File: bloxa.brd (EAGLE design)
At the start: 24.9 x 33.6 mm, 87 parts, among them CON1 PINHEAD_1X02-2.54, CON7 CON-4P-JST_GH-RA, CON8 CON-4P-JST_GH-RA, IC1 TPD3S014DBVR-SOT23-6, IC3 TJA1051, IC6 MCP9700, Q13 BUK9K6R2-40E,115, Q14 BUK9K6R2-40E,115, Q15 BUK9K6R2-40E,115

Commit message: updates
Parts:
- moved CON7 3.00 mm to (-4.50, -12.5)
- moved CON8 3.00 mm to (4.50, -12.5)
- renumbered PAD42 to BAT-, PAD43 to BAT+
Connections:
- removed net CAN2_LED1: R9.1
- removed net LED_BLUE: R11.2
- removed net LED_GREEN: R12.2
- removed net LED_RED: R13.2
- removed net N$3: BAT+.P$1, D1.C, D2.C
- net CAN1_LED: now also R9.1
- net GPIO1: now also CON1.2
- net PGND: now also CON1.1
- net RGB_LED_B: now also R11.2
- net RGB_LED_G: now also R12.2
- net RGB_LED_R: now also R13.2
- net VDC: now also BAT+.P$1, D1.C, D2.C

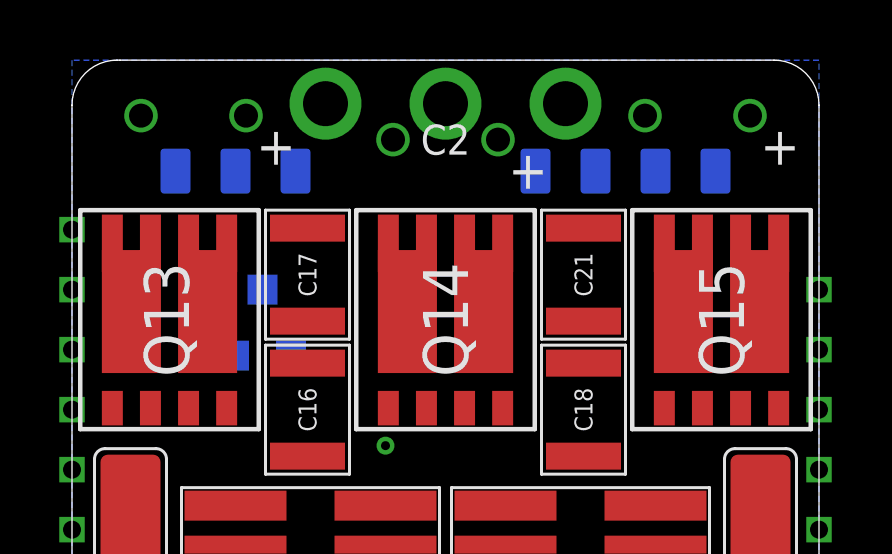
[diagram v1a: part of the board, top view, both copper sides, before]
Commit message: proper DRC and some polygons
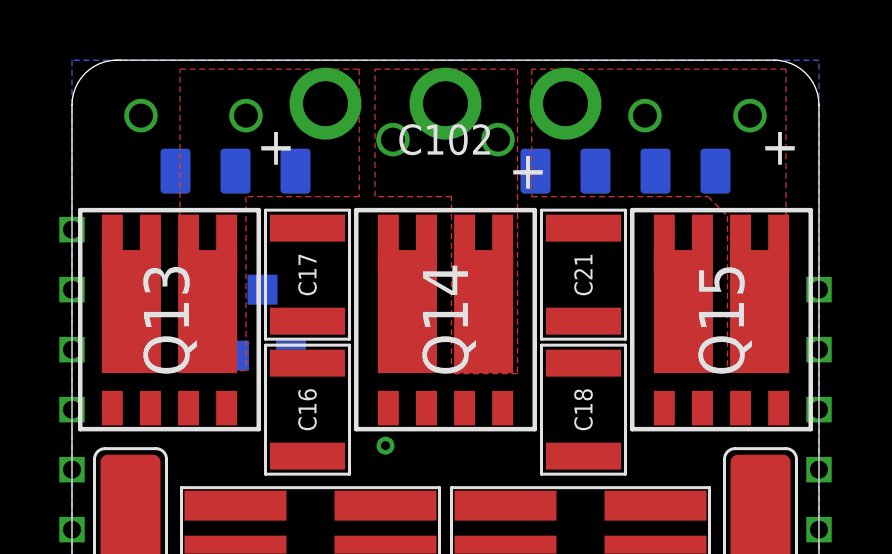
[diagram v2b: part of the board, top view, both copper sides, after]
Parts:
- renumbered C1 to C101, C2 to C102, C6 to C100
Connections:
- removed net VBAT: PAD3.P$1
- net VDC: now also PAD3.P$1
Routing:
- net VDDA: track 25.6 -> 0.00 mm
- net N$2: track 1.53 -> 0.00 mm
- net AGND: track 1.53 -> 0.00 mm
- added copper zone on layer 15, net PGND
- added copper zone on layer 1, net PHASE_A
- added copper zone on layer 1, net PHASE_B
- added copper zone on layer 1, net PHASE_C
- added copper zone on layer 2, net VDC
- removed copper zone on layer 15, net AGND
- removed copper zone on layer 2, net AGND
- removed copper zone on layer 4, net AGND
- removed copper zone on layer 15, net GND
- removed copper zone on layer 2, net GND
- removed copper zone on layer 4, net GND
- removed copper zone on layer 3, net VBAT
- removed copper zone on layer 2, net VDDA
- removed copper zone on layer 3, net VDD_3V3
- removed copper zone on layer 4, net VDD_5V

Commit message: updates
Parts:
- moved S2 16.2 mm to (14.2, 5.62)
- moved BAT- 1.20 mm to (-10.5, 2.30)
- moved A 0.05 mm to (-4.00, 17.1)
- moved B 0.05 mm to (0.00, 17.1)
- moved C 0.05 mm to (4.00, 17.1)
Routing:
- net N$27: track 0.00 -> 1.31 mm, vias 0 -> 1
- net N$24: track 0.00 -> 1.10 mm, vias 0 -> 1
- net PHASE_B: track 0.00 -> 0.45 mm, vias 0 -> 8
- net PHASE_A: track 0.00 -> 0.45 mm, vias 0 -> 8
- added copper zone on layer 1, net PHASE_A_GND

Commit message: more polygones
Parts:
- moved IC6 5.89 mm to (-10.2, 14.1)
- moved R26 0.12 mm to (-4.50, 2.38)
- moved R33 0.12 mm to (4.50, 2.38)
- moved BAT- 0.08 mm to (-10.6, 2.27)
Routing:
- net PHASE_A_CURRENT_SHUNT_N: track 0.00 -> 3.83 mm, vias 0 -> 1
- net PHASE_A_CURRENT_SHUNT_P: track 0.00 -> 3.70 mm, vias 0 -> 1
- net PHASE_B_CURRENT_SHUNT_P: track 0.00 -> 3.23 mm, vias 0 -> 1
- net PHASE_B_CURRENT_SHUNT_N: track 0.00 -> 3.23 mm, vias 0 -> 1
- net PHASE_A: vias 8 -> 7
- added copper zone on layer 1, net PGND
- added copper zone on layer 16, net PGND
- added copper zone on layer 1, net PHASE_B_GND
- added copper zone on layer 1, net VDC
- removed copper zone on layer 16, net GND

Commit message: some progress
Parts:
- moved BAT- 21.1 mm to (10.5, 2.20)
- moved BAT+ 21.0 mm to (-10.5, 2.20)
- moved R35 18.6 mm to (-8.45, 3.00), flipped to the bottom, turned to 180 degrees
- moved R36 16.3 mm to (-8.45, -1.35), flipped to the bottom, turned to 180 degrees
- moved R31 14.3 mm to (-8.45, 8.40), flipped to the bottom, turned to 180 degrees
- moved R32 12.9 mm to (-8.45, 7.05), flipped to the bottom, turned to 180 degrees
- moved R37 11.6 mm to (-8.45, -2.70), flipped to the bottom, turned to 180 degrees
- moved R11 10.5 mm to (16.7, -10.4)
- moved R12 10.5 mm to (18.9, -10.4)
- moved R13 10.5 mm to (17.8, -10.4)
- moved IC6 10.2 mm to (0.00, 14.1)
- moved R34 9.19 mm to (-8.45, 4.35), flipped to the bottom, turned to 180 degrees
- moved CON1 2.38 mm to (8.93, -7.12)
- moved D2 0.55 mm to (8.55, -2.05)
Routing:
- net PHASE_C: track 0.00 -> 30.7 mm
- net N$29: track 0.00 -> 24.2 mm, vias 0 -> 1
- net N$28: track 0.00 -> 22.1 mm, vias 0 -> 1
- net PHASE_B: track 0.45 -> 17.9 mm
- net N$31: track 0.00 -> 14.2 mm, vias 0 -> 1
- net N$30: track 0.00 -> 12.0 mm, vias 0 -> 1
- net PHASE_A_GATE_HIGH: track 0.00 -> 7.89 mm
- net PHASE_B_GATE_LOW: track 0.00 -> 6.95 mm
- net PHASE_A: track 0.45 -> 5.96 mm, vias 7 -> 8
- net PHASE_B_GND: track 0.00 -> 4.57 mm
- net PHASE_A_GATE_LOW: track 0.00 -> 4.51 mm
- net PHASE_C_GATE_HIGH: track 0.00 -> 4.18 mm
- net PHASE_B_GATE_HIGH: track 0.00 -> 3.77 mm
- net PHASE_A_CURRENT_SHUNT_N: track 3.83 -> 2.10 mm
- net PHASE_A_CURRENT_SHUNT_P: track 3.70 -> 2.10 mm
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
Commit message: some more progress
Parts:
- removed IC3: TJA1051, myxa_masterlib:SOT782-1
- added IC2: TJA1051(X)/3-SO8, serial_interfaces:SOIC8
- added U$13: (no value), pixhawk_esc_1.5_master_lib:ZUBAX_LOGO_5X10
- added U$2: (no value), logo:DRAGON-18X7
- moved C15 20.5 mm to (-2.25, 13.4), flipped to the bottom, turned to 270 degrees
- moved C22 19.7 mm to (1.30, 11.0), flipped to the bottom, turned to 90 degrees
- moved R30 18.4 mm to (0.10, 11.2), flipped to the bottom, turned to 90 degrees
- moved R12 12.2 mm to (7.20, -6.88)
- moved R11 11.2 mm to (6.10, -6.85), turned to 90 degrees
- moved R13 10.1 mm to (8.30, -6.88)
- moved R9 8.46 mm to (-10.4, -12.5)
- moved LED1 7.47 mm to (-10.4, -13.8), flipped to the top, turned to 180 degrees
- moved C11 7.40 mm to (-9.95, -6.10)
- moved S2 6.55 mm to (9.80, 0.80)
- moved C5 5.95 mm to (0.50, -6.67), turned to 90 degrees
- moved C7 4.29 mm to (1.90, -6.67), turned to 90 degrees
- moved C3 4.26 mm to (-0.75, -6.45), turned to 270 degrees
- moved IC1 3.20 mm to (1.48, -3.62)
- moved C9 3.04 mm to (3.30, -6.67), turned to 90 degrees
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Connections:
- removed net TEMP_SENS: PAD20.P$1
- new net N$2: IC2.8
- net CAN1_RX: now also IC2.4; no longer IC3.4
- net CAN1_TX: now also IC2.1; no longer IC3.1
- net GND: now also IC2.2; no longer IC3.2, IC3.8, IC3.PAD
- net N$22: now also IC2.7; no longer IC3.7
- net N$23: now also IC2.6; no longer IC3.6
- net TEMPERATURE_SENSOR: now also PAD20.P$1
- net VDD_5V: now also IC2.3, IC2.5; no longer IC3.3, IC3.5
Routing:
- net CAN1_RX: track 0.00 -> 33.6 mm, vias 0 -> 1
- net CAN1_VDD: track 0.00 -> 29.5 mm
- net CAN1_TX: track 0.00 -> 28.9 mm, vias 0 -> 1
- net PHASE_B_CURRENT_SHUNT_P: track 2.10 -> 25.1 mm
- net PHASE_B_CURRENT_SHUNT_N: track 2.10 -> 25.1 mm
- net PHASE_A_CURRENT_SHUNT_P: track 2.10 -> 21.5 mm
- net PHASE_A_CURRENT_SHUNT_N: track 2.10 -> 21.0 mm
- net N$22: track 0.00 -> 18.3 mm
- net N$23: track 0.00 -> 16.9 mm
- net RGB_LED_B: track 0.00 -> 11.2 mm
- net VDD_5V: track 0.00 -> 10.3 mm, vias 0 -> 1
- net N$60: track 0.00 -> 8.53 mm
- net RGB_LED_G: track 0.00 -> 8.37 mm
- net N$59: track 0.00 -> 8.27 mm
- net N$58: track 0.00 -> 6.45 mm
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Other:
- board text removed: "HIGH_SIDE"
- board text removed: "LOW_SIDE"

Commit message: some progress
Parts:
- moved C15 6.02 mm to (-1.35, 7.50)
- moved IC6 5.98 mm to (0.80, 8.12)
- moved R31 2.49 mm to (-8.22, 5.92), turned to 0 degrees
- moved R30 1.38 mm to (1.40, 11.7), turned to 0 degrees
- moved C22 0.59 mm to (1.15, 10.4), turned to 180 degrees
- moved R32 0.23 mm to (-8.22, 7.03)
- moved CON1 0.22 mm to (10.4, -8.60)
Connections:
- net GND: no longer PAD2.P$1
- net PGND: now also PAD2.P$1
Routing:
- net PHASE_B_GND: track 4.57 -> 17.0 mm, vias 0 -> 1
- net PHASE_C_GATE_LOW: track 0.00 -> 6.06 mm
- net PHASE_A_GATE_HIGH: track 7.89 -> 13.2 mm
- net VDC: track 0.00 -> 3.79 mm, vias 52 -> 49
- net PHASE_A: track 5.96 -> 9.06 mm, vias 8 -> 9
- net N$27: track 0.25 -> 3.12 mm, vias 0 -> 1
- net PHASE_B_GATE_LOW: track 6.95 -> 5.18 mm
- net CAN1_RX: track 33.6 -> 32.0 mm
- net N$1: track 3.33 -> 4.69 mm
- net N$24: track 0.37 -> 1.25 mm, vias 0 -> 1
- net PHASE_C: track 30.3 -> 29.6 mm
- net CAN1_TX: track 28.9 -> 28.2 mm

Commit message: more polygones updates
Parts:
- moved R34 0.07 mm to (-8.38, 4.35)
- moved R35 0.07 mm to (-8.38, 3.00)
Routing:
- net PHASE_C_GND: track 0.00 -> 27.5 mm
- net BEC_ENABLE_OUT: track 0.00 -> 16.0 mm, vias 0 -> 1
- net PHASE_A_GATE_HIGH: track 13.2 -> 5.56 mm
- net PHASE_B_GATE_LOW: track 5.18 -> 0.39 mm
- net PHASE_A: track 9.06 -> 5.96 mm, vias 9 -> 16
- net VDC: track 3.79 -> 5.12 mm
- net N$24: track 1.25 -> 2.22 mm
- net PHASE_B: track 17.9 -> 18.4 mm, vias 8 -> 16
- net PHASE_C: vias 8 -> 16
- added copper zone on layer 2, net PHASE_A
- added copper zone on layer 2, net PHASE_B
- added copper zone on layer 2, net PHASE_C
